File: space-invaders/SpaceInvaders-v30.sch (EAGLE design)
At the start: 26 parts, among them J2-J4 TM4C123GXL, J3-J1 TM4C123GXL, J5 NOKIA_5110, J6 NOKIA_5110, J7 9V, U1 LM7805CT

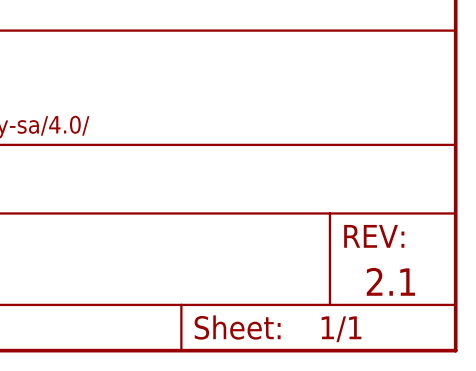
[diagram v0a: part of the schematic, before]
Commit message: Add versions to file names & Edit stuff
Add versions to file names.
Center Nokia5110 & Edit traces thereof.
Add holes for 9V battery's wires to come through.
v2.1: Replace "SpaceInvaders," "by PhiL," and the sprite icon by Top &
Bottom layers.
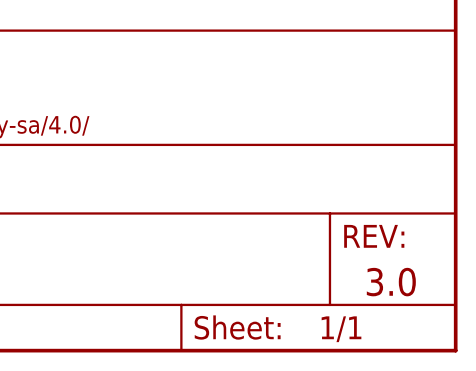
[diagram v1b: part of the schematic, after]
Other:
- note added: "3.0"
- note removed: "2.1"
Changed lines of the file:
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@@
 <plain>
 <text x="172.72" y="12.7" size="3.048" layer="94" font="vector" align="center-left">Phi Luu</text>
-<text x="238.76" y="7.62" size="3.048" layer="94" font="vector" align="center-left">2.1</text>
+<text x="238.76" y="7.62" size="3.048" layer="94" font="vector" align="center-left">3.0</text>
 <text x="134.62" y="147.32" size="1.778" layer="96" font="vector" rot="R90">PB0</text>
 <text x="132.08" y="147.32" size="1.778" layer="96" font="vector" rot="R90">PB1</text>
